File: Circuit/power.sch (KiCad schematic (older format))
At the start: 22 parts, among them Q202 FDN340P, Q203 FDN340P, SW1 ON/OFF, U201 CN3063, U202 MCP6002, U3 LXDC2XQ

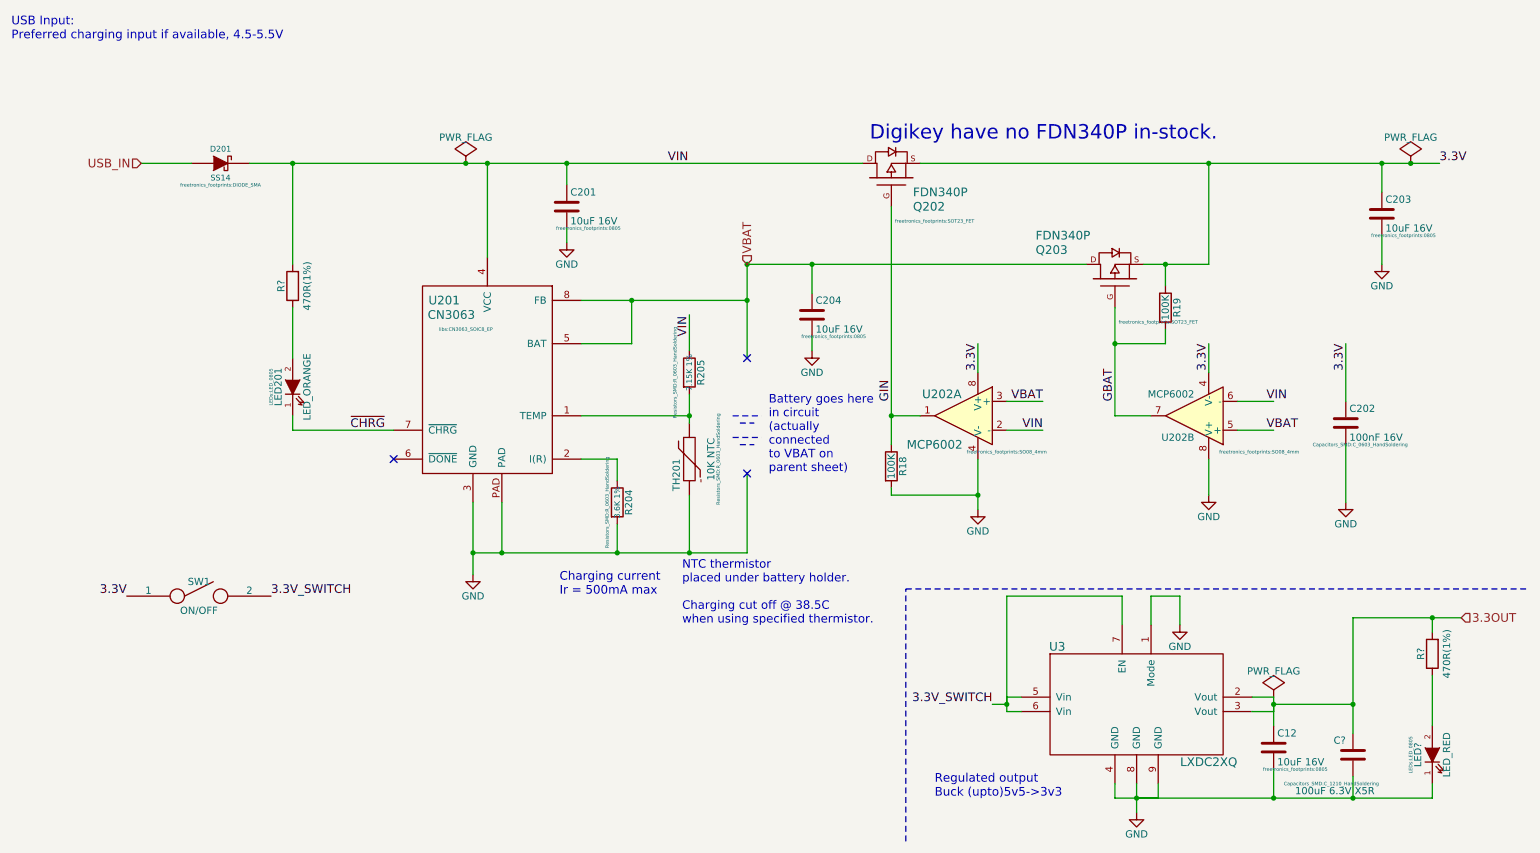
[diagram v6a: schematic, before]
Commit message: Updated alligator clips.
Some basic placement
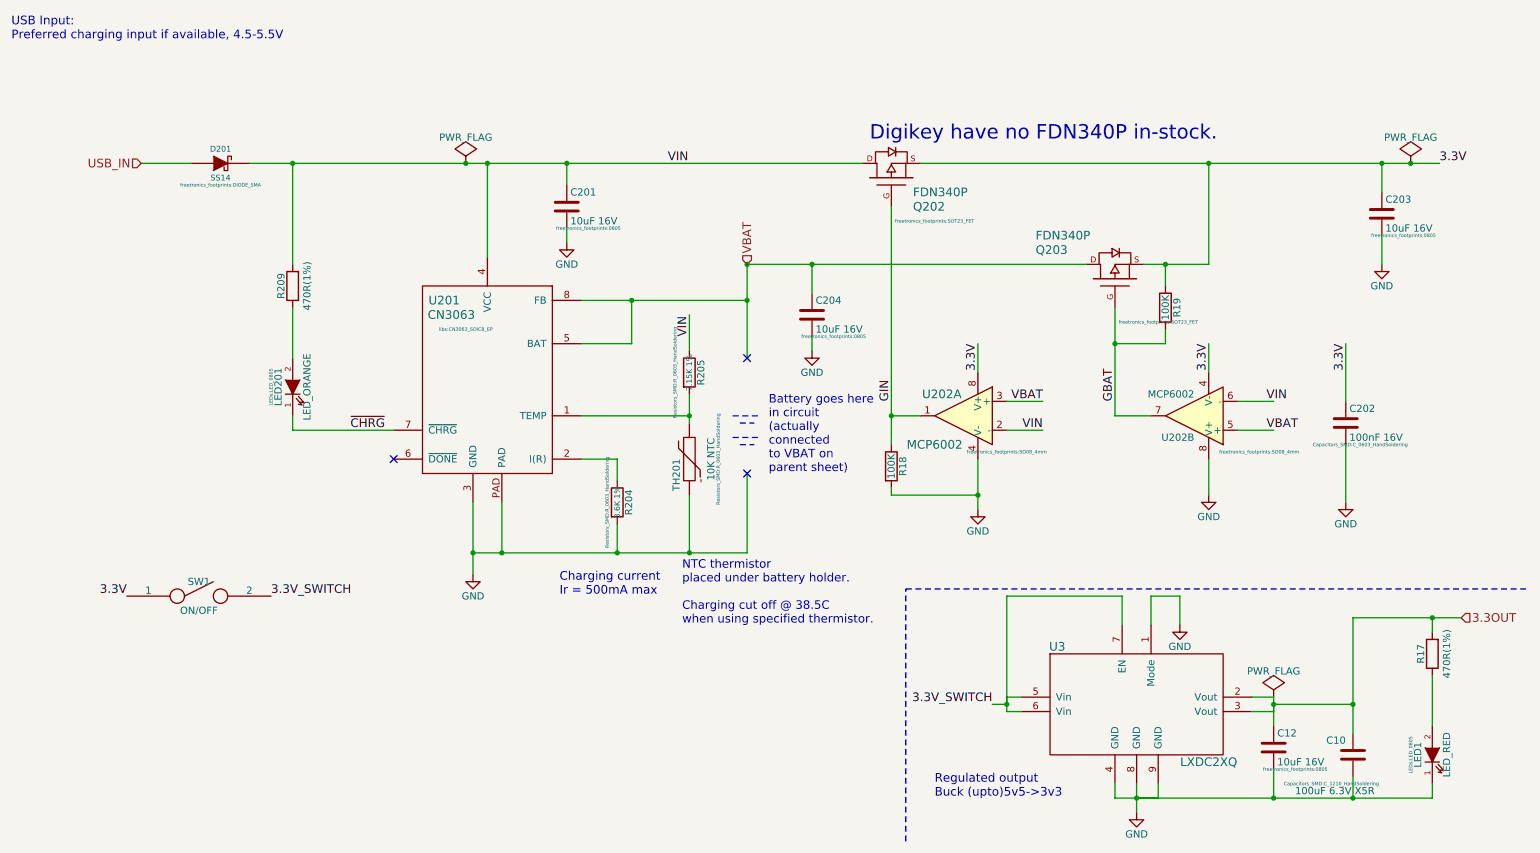
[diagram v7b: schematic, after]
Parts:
- U3: footprint (none) -> libs:LXDC2XQ
- gave numbers to parts that had none: 4
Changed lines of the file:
@@
 USB_IN
 $Comp
-L GND #PWR031
+L GND #PWR027
 U 1 1 563C4E24
 P 3950 4650
-F 0 "#PWR031" H 3950 4400 50  0001 C CNN
+F 0 "#PWR027" H 3950 4400 50  0001 C CNN
 F 1 "GND" H 3950 4500 50  0000 C CNN
 F 2 "" H 3950 4650 60  0000 C CNN
@@
 Charging current\nIr = 500mA max
 $Comp
-L GND #PWR032
+L GND #PWR028
 U 1 1 56417FB3
 P 7450 4200
-F 0 "#PWR032" H 7450 3950 50  0001 C CNN
+F 0 "#PWR028" H 7450 3950 50  0001 C CNN
 F 1 "GND" H 7450 4050 50  0000 C CNN
 F 2 "" H 7450 4200 60  0000 C CNN
@@
 3.3OUT
 $Comp
-L GND #PWR033
+L GND #PWR029
 U 1 1 5641AA9F
 P 10250 2500
-F 0 "#PWR033" H 10250 2250 50  0001 C CNN
+F 0 "#PWR029" H 10250 2250 50  0001 C CNN
 F 1 "GND" H 10250 2350 50  0000 C CNN
 F 2 "" H 10250 2500 60  0000 C CNN
@@
 $EndComp
 $Comp
-L GND #PWR034
+L GND #PWR030
 U 1 1 5642C1C1
 P 9050 4100
-F 0 "#PWR034" H 9050 3850 50  0001 C CNN
+F 0 "#PWR030" H 9050 3850 50  0001 C CNN
 F 1 "GND" H 9050 3950 50  0000 C CNN
 F 2 "" H 9050 4100 60  0000 C CNN
@@
 VIN
 $Comp
-L C C?
+L C C10
 U 1 1 5642CCBE
 P 10050 5900
-F 0 "C?" H 10100 5800 50  0000 L CNN
+F 0 "C10" H 10100 5800 50  0000 L CNN
 F 1 "100uF 6.3V X5R" H 9900 6150 50  0000 L CNN
 F 2 "Capacitors_SMD:C_1210_HandSoldering" H 10200 6100 24  0000 C CNN
@@
 $EndComp
 $Comp
-L PWR_FLAG #FLG035
+L PWR_FLAG #FLG031
 U 1 1 5642D1CE
 P 10450 1800
-F 0 "#FLG035" H 10450 1895 50  0001 C CNN
+F 0 "#FLG031" H 10450 1895 50  0001 C CNN
 F 1 "PWR_FLAG" H 10450 1980 50  0000 C CNN
 F 2 "" H 10450 1800 60  0000 C CNN
@@
 $EndComp
 $Comp
-L PWR_FLAG #FLG036
+L PWR_FLAG #FLG032
 U 1 1 5642D5A3
 P 3900 1800
-F 0 "#FLG036" H 3900 1895 50  0001 C CNN
+F 0 "#FLG032" H 3900 1895 50  0001 C CNN
 F 1 "PWR_FLAG" H 3900 1980 50  0000 C CNN
 F 2 "" H 3900 1800 60  0000 C CNN
@@
 $EndComp
 $Comp
-L GND #PWR037
+L GND #PWR033
 U 1 1 5642DA26
 P 10000 4150
-F 0 "#PWR037" H 10000 3900 50  0001 C CNN
+F 0 "#PWR033" H 10000 3900 50  0001 C CNN
 F 1 "GND" H 10000 4000 50  0000 C CNN
 F 2 "" H 10000 4150 60  0000 C CNN
@@
 $EndComp
 $Comp
-L GND #PWR038
+L GND #PWR034
 U 1 1 5642CE9D
 P 4600 2350
-F 0 "#PWR038" H 4600 2100 50  0001 C CNN
+F 0 "#PWR034" H 4600 2100 50  0001 C CNN
 F 1 "GND" H 4600 2200 50  0000 C CNN
 F 2 "" H 4600 2350 60  0000 C CNN
@@
 NTC thermistor\nplaced under battery holder.\n\nCharging cut off @ 38.5C\nwhen using specified thermistor.
 $Comp
-L GND #PWR039
+L GND #PWR035
 U 1 1 566FA00B
 P 6300 3100
-F 0 "#PWR039" H 6300 2850 50  0001 C CNN
+F 0 "#PWR035" H 6300 2850 50  0001 C CNN
 F 1 "GND" H 6300 2950 50  0000 C CNN
 F 2 "" H 6300 3100 60  0000 C CNN
@@
 $EndComp
 $Comp
-L GND #PWR040
+L GND #PWR036
 U 1 1 5812C93A
 P 8550 6300
-F 0 "#PWR040" H 8550 6050 50  0001 C CNN
+F 0 "#PWR036" H 8550 6050 50  0001 C CNN
 F 1 "GND" H 8550 6150 50  0000 C CNN
 F 2 "" H 8550 6300 60  0000 C CNN
@@
 $EndComp
 $Comp
-L GND #PWR041
+L GND #PWR037
 U 1 1 5812E212
 P 8850 5000
-F 0 "#PWR041" H 8850 4750 50  0001 C CNN
+F 0 "#PWR037" H 8850 4750 50  0001 C CNN
 F 1 "GND" H 8850 4850 50  0000 C CNN
 F 2 "" H 8850 5000 60  0000 C CNN
@@
 F 0 "U3" H 8000 5950 60  0000 C CNN
 F 1 "LXDC2XQ" H 9050 5150 60  0000 C CNN
-F 2 "" H 7900 5850 60  0001 C CNN
+F 2 "libs:LXDC2XQ" H 7900 5850 60  0001 C CNN
 F 3 "http://power.murata.com/data/power/LXDC2XQ_Series_datasheet.pdf" H 8000 5950 60  0001 C CNN
 F 4 "http://www.digikey.com.au/product-detail/en/murata-electronics-north-america/LXDC2XQ33A-254/490-12573-1-ND/5797558" H 8100 6050 60  0001 C CNN "Digikey URL"
@@
 NoConn ~ 5850 3950
 $Comp
-L R R?
+L R R209
 U 1 1 5820F348
 P 2700 2650
-F 0 "R?" V 2780 2650 50  0000 C CNN
+F 0 "R209" V 2780 2650 50  0000 C CNN
 F 1 "470R(1%)" V 2600 2650 50  0000 C CNN
 F 2 "Resistors_SMD:R_0603_HandSoldering" V 2630 2650 50  0001 C CNN
@@
 Connection ~ 9500 6200
 $Comp
-L PWR_FLAG #FLG?
+L PWR_FLAG #FLG038
 U 1 1 58217320
 P 9500 5500
-F 0 "#FLG?" H 9500 5595 50  0001 C CNN
+F 0 "#FLG038" H 9500 5595 50  0001 C CNN
 F 1 "PWR_FLAG" H 9500 5680 50  0000 C CNN
 F 2 "" H 9500 5500 60  0000 C CNN
@@
 $EndComp
 $Comp
-L LED LED?
+L LED LED1
 U 1 1 5822B84F
 P 10600 5900
-F 0 "LED?" H 10600 6000 50  0000 C CNN
+F 0 "LED1" H 10600 6000 50  0000 C CNN
 F 1 "LED_RED" H 10600 5800 50  0000 C CNN
 F 2 "LEDs:LED_0805" H 10600 6050 24  0000 C CNN
@@
 	10600 5350 10600 5700
 $Comp
-L R R?
+L R R17
 U 1 1 5822B85B
 P 10600 5200
-F 0 "R?" V 10680 5200 50  0000 C CNN
+F 0 "R17" V 10680 5200 50  0000 C CNN
 F 1 "470R(1%)" V 10500 5200 50  0000 C CNN
 F 2 "Resistors_SMD:R_0603_HandSoldering" V 10530 5200 50  0001 C CNN
